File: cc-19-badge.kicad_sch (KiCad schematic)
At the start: 1 part

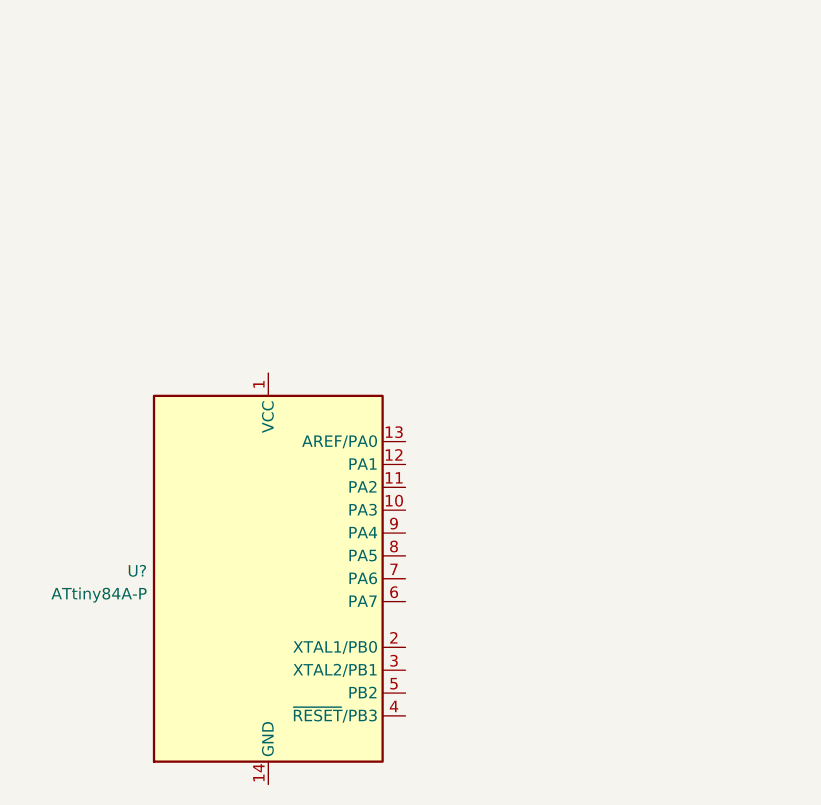
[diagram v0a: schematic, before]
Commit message: 9 make the pcb look like a beer can (#11)
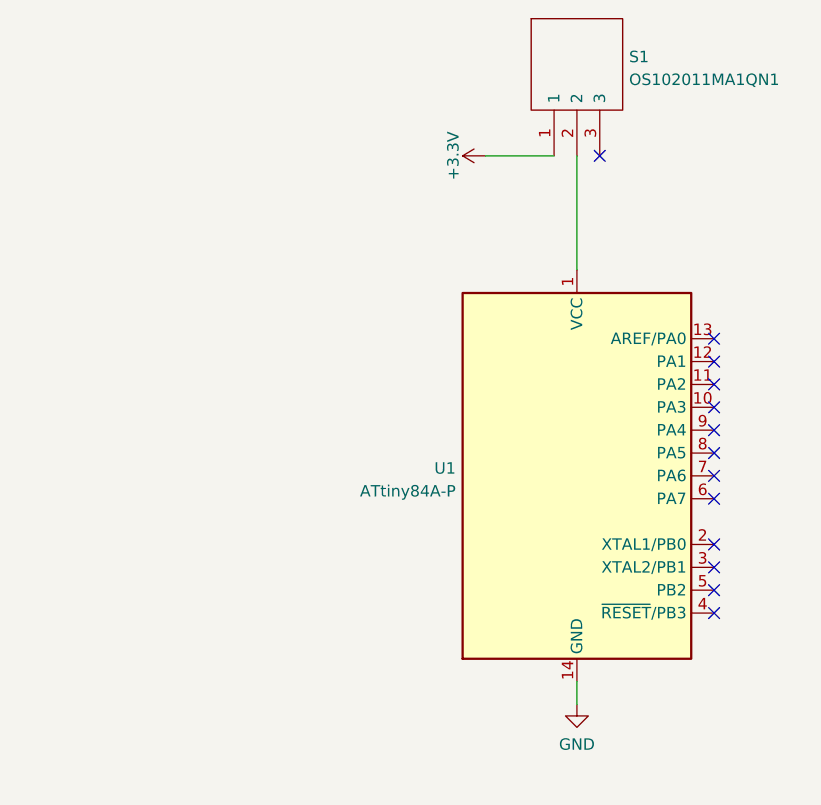
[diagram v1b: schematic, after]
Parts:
- removed U?: ATtiny84A-P, Package_DIP:DIP-14_W7.62mm, symbol MCU_Microchip_ATtiny:ATtiny84A-P
- added S1: OS102011MA1QN1, OS102011MA1QN1, symbol OS102011MA1QN1:OS102011MA1QN1
- added U1: ATtiny84A-P, Package_DIP:DIP-14_W7.62mm, symbol MCU_Microchip_ATtiny:ATtiny84A-P
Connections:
- new net: S1.2, U1.1 (VCC)
- new net +3.3V: S1.1
- new net GND: U1.14 (GND)
- no-connect marks 0 -> 13
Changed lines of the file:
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@@
 (kicad_sch (version 20211123) (generator eeschema)
   (paper "A4")
-  (symbol (lib_id "MCU_Microchip_ATtiny:ATtiny84A-P") (at 90.17 107.95 0) (unit 1)
+  (no_connect (at 139.7 96.52))
+  (no_connect (at 139.7 106.68))
+  (no_connect (at 139.7 81.28))
+  (no_connect (at 139.7 99.06))
+  (no_connect (at 139.7 109.22))
+  (no_connect (at 139.7 104.14))
+  (no_connect (at 139.7 91.44))
+  (no_connect (at 139.7 86.36))
+  (no_connect (at 139.7 93.98))
+  (no_connect (at 127 60.96))
+  (no_connect (at 139.7 88.9))
+  (no_connect (at 139.7 83.82))
+  (no_connect (at 139.7 111.76))
+  (wire (pts (xy 114.3 60.96) (xy 121.92 60.96))
+    (stroke (width 0) (type default) (color 0 0 0 0))
+  )
+  (wire (pts (xy 124.46 60.96) (xy 124.46 73.66))
+    (stroke (width 0) (type default) (color 0 0 0 0))
+  )
+  (wire (pts (xy 124.46 119.38) (xy 124.46 121.92))
+    (stroke (width 0) (type default) (color 0 0 0 0))
+  )
+  (symbol (lib_id "power:+3.3V") (at 114.3 60.96 90) (unit 1)
+    (in_bom yes) (on_board yes)
+    (property "Reference" "#PWR0102" (id 0) (at 118.11 60.96 0)
+      (effects (font (size 1.27 1.27)) hide)
+    )
+    (property "Value" "+3.3V" (id 1) (at 110.7242 60.96 0))
+    (property "Footprint" "" (id 2) (at 114.3 60.96 0)
+      (effects (font (size 1.27 1.27)) hide)
+    )
+    (property "Datasheet" "" (id 3) (at 114.3 60.96 0)
+      (effects (font (size 1.27 1.27)) hide)
+    )
+    (pin "1")
+  )
+  (symbol (lib_id "OS102011MA1QN1:OS102011MA1QN1") (at 121.92 60.96 0) (unit 1)
     (in_bom yes) (on_board yes) (fields_autoplaced)
-    (property "Reference" "U?" (id 0) (at 76.7081 107.1153 0)
+    (property "Reference" "S1" (id 0) (at 130.2512 49.9653 0)
+      (effects (font (size 1.27 1.27)) (justify left))
+    )
+    (property "Value" "OS102011MA1QN1" (id 1) (at 130.2512 52.5022 0)
+      (effects (font (size 1.27 1.27)) (justify left))
+    )
+    (property "Footprint" "OS102011MA1QN1" (id 2) (at 130.81 45.72 0)
+      (effects (font (size 1.27 1.27)) (justify left) hide)
+    )
+    (property "Datasheet" "http://www.ckswitches.com/media/1428/os.pdf" (id 3) (at 130.81 48.26 0)
+      (effects (font (size 1.27 1.27)) (justify left) hide)
+    )
+    (property "Description" "Switch Slide Right Angle SPDT 0.1A 12VDC Through Hole Slide Switch SPDT On-On 0.1 A@ 12 V dc Slide" (id 4) (at 130.81 50.8 0)
+      (effects (font (size 1.27 1.27)) (justify left) hide)
+    )
+    (property "Height" "" (id 5) (at 130.81 53.34 0)
+      (effects (font (size 1.27 1.27)) (justify left) hide)
+    )
+    (property "Mouser Part Number" "611-OS102011MA1QN1" (id 6) (at 130.81 55.88 0)
+      (effects (font (size 1.27 1.27)) (justify left) hide)
+    )
+    (property "Mouser Price/Stock" "https://www.mouser.co.uk/ProductDetail/CK/OS102011MA1QN1?qs=WtljUlYws5R6MUgHcLkz4w%3D%3D" (id 7) (at 130.81 58.42 0)
+      (effects (font (size 1.27 1.27)) (justify left) hide)
+    )
+    (property "Manufacturer_Name" "C & K COMPONENTS" (id 8) (at 130.81 60.96 0)
+      (effects (font (size 1.27 1.27)) (justify left) hide)
+    )
+    (property "Manufacturer_Part_Number" "OS102011MA1QN1" (id 9) (at 130.81 63.5 0)
+      (effects (font (size 1.27 1.27)) (justify left) hide)
+    )
+    (pin "1")
+    (pin "2")
+    (pin "3")
+  )
+  (symbol (lib_id "power:GND") (at 124.46 121.92 0) (unit 1)
+    (in_bom yes) (on_board yes) (fields_autoplaced)
+    (property "Reference" "#PWR0101" (id 0) (at 124.46 128.27 0)
+      (effects (font (size 1.27 1.27)) hide)
+    )
+    (property "Value" "GND" (id 1) (at 124.46 126.3634 0))
+    (property "Footprint" "" (id 2) (at 124.46 121.92 0)
+      (effects (font (size 1.27 1.27)) hide)
+    )
+    (property "Datasheet" "" (id 3) (at 124.46 121.92 0)
+      (effects (font (size 1.27 1.27)) hide)
+    )
+    (pin "1")
+  )
+  (symbol (lib_id "MCU_Microchip_ATtiny:ATtiny84A-P") (at 124.46 96.52 0) (unit 1)
+    (in_bom yes) (on_board yes) (fields_autoplaced)
+    (property "Reference" "U1" (id 0) (at 110.9981 95.6853 0)
       (effects (font (size 1.27 1.27)) (justify right))
     )
-    (property "Value" "ATtiny84A-P" (id 1) (at 76.7081 109.6522 0)
+    (property "Value" "ATtiny84A-P" (id 1) (at 110.9981 98.2222 0)
       (effects (font (size 1.27 1.27)) (justify right))
     )
-    (property "Footprint" "Package_DIP:DIP-14_W7.62mm" (id 2) (at 90.17 107.95 0)
+    (property "Footprint" "Package_DIP:DIP-14_W7.62mm" (id 2) (at 124.46 96.52 0)
       (effects (font (size 1.27 1.27) italic) hide)
     )
-    (property "Datasheet" "http://ww1.microchip.com/downloads/en/DeviceDoc/doc8183.pdf" (id 3) (at 90.17 107.95 0)
+    (property "Datasheet" "http://ww1.microchip.com/downloads/en/DeviceDoc/doc8183.pdf" (id 3) (at 124.46 96.52 0)
       (effects (font (size 1.27 1.27)) hide)
     )
@@
   )
   (symbol_instances
-    (path "/c53d2f4d-cfa3-4e34-aa9d-268fb6765344"
-      (reference "U?") (unit 1) (value "ATtiny84A-P") (footprint "Package_DIP:DIP-14_W7.62mm")
+    (path "/28701a8b-e9e9-4466-8fbd-2ff8d8c7af4f"
+      (reference "#PWR0101") (unit 1) (value "GND") (footprint "")
+    )
+    (path "/03b8bb26-888a-4324-a542-2f053d7430d1"
+      (reference "#PWR0102") (unit 1) (value "+3.3V") (footprint "")
+    )
+    (path "/040f8082-76ef-4eb1-ac5d-3018b40eb874"
+      (reference "S1") (unit 1) (value "OS102011MA1QN1") (footprint "OS102011MA1QN1")
+    )
+    (path "/b2e1ea54-795e-4622-b6af-e8674d527d3d"
+      (reference "U1") (unit 1) (value "ATtiny84A-P") (footprint "Package_DIP:DIP-14_W7.62mm")
     )
   )

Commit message: 20 update schematic (#22)
Co-authored-by: github-actions <github-actions@github.com>
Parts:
- added C1, C2: 100nF, third-party-schematics:K104K15X7RF5TH5, symbol K104K15X7RF5TH5:K104K15X7RF5TH5
- added C_RST1: 10uF, third-party-schematics:CAPPRD200W52D500H1250, symbol 860020372001:860020372001
- added IC1: ST25DV04KC-IE8S3, third-party-schematics:SOIC127P600X175-8N, symbol ST25DV04KC-IE8S3:ST25DV04KC-IE8S3
- added ISP1: Conn_02x03_Odd_Even, Connector_PinHeader_2.54mm:PinHeader_2x03_P2.54mm_Vertical, symbol Connector_Generic:Conn_02x03_Odd_Even
- added SCL_PULL1, SDA_PULL1: R_Small, symbol Device:R_Small
- S1: footprint OS102011MA1QN1 -> third-party-schematics:OS102011MA1QN1; Mouser Price/Stock https://www.mouser.co.uk/ProductDetail/CK/OS102011MA1QN1?qs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 -> https://www.mouser.com/ProductDetail/CK/OS102011MA1QN1?qs=W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
- U1: Mouser Part Number (none) -> 556-ATTINY84A-PU; Mouser Price/Stock (none) -> https://www.mouser.com/ProductDetail/Microchip-Technology-A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
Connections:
- net +3.3V: now also S1.2, U1.1 (VCC), C1.1, ISP1.2 (Pin_2); no longer S1.1
- net GND: now also C1.2, C2.2, C_RST1.2, IC1.4 (VSS), ISP1.6 (Pin_6)
- net at U1.11 (PA2): now also IC1.7 (GPO_(OPEN_DRAIN))
- net RST: now reaches U1.4 (~{RESET}/PB3)
- net RST: now also C_RST1.1, ISP1.5 (Pin_5)
- net MOSI: now reaches U1.7 (PA6)
- net MOSI: now also IC1.6 (SCL), ISP1.4 (Pin_4), SCL_PULL1.2
- net MISO: now reaches U1.8 (PA5)
- net MISO: now also ISP1.1 (Pin_1)
- net SCK: now reaches U1.9 (PA4)
- net SCK: now also IC1.5 (SDA), ISP1.3 (Pin_3), SDA_PULL1.2
- new net: C2.1, IC1.8 (VCC)
- new net +BATT: S1.1
- no-connect marks 13 -> 8
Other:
- moved on the sheet: S1, U1

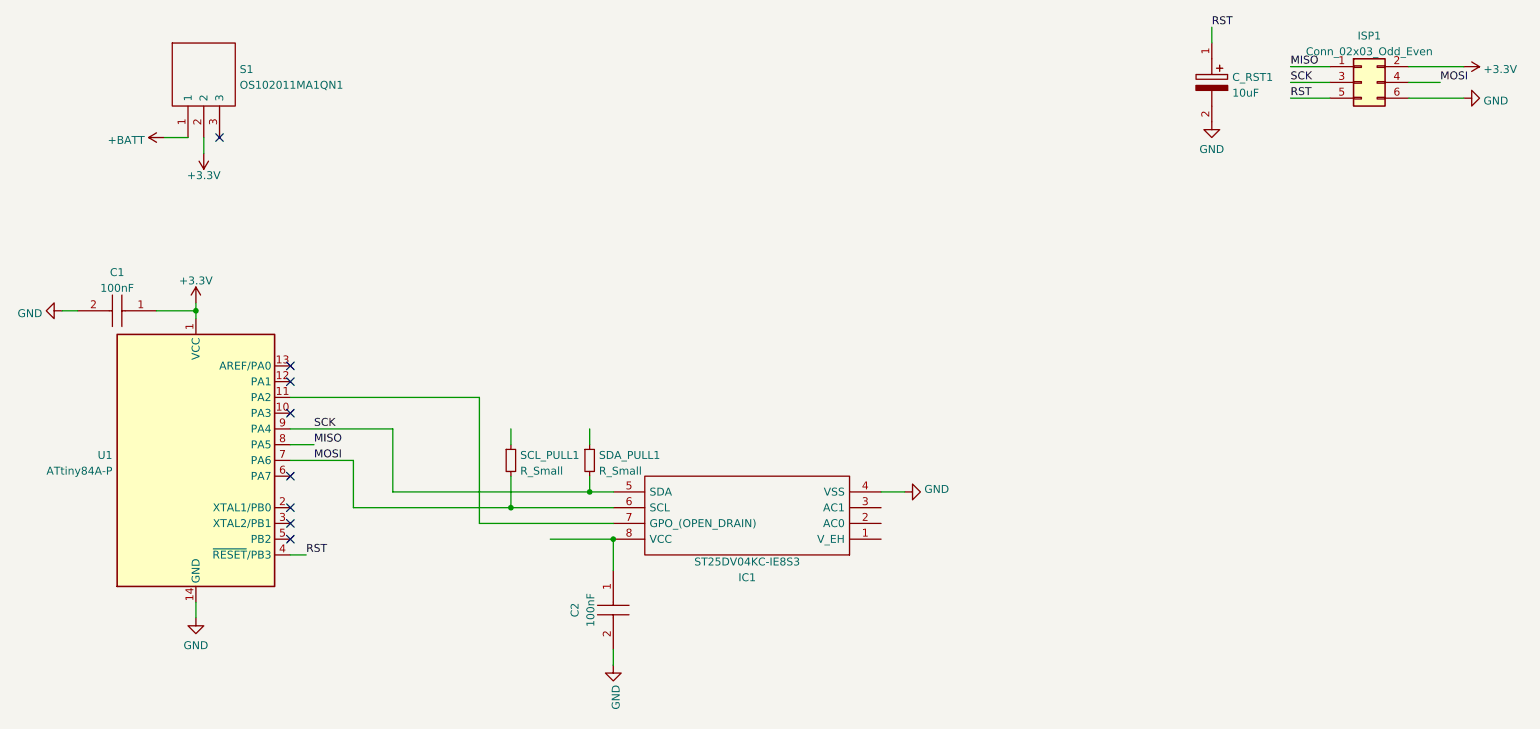
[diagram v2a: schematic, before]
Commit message: Add a 13.56 mhz antenna of questionable effectiveness  (#25)
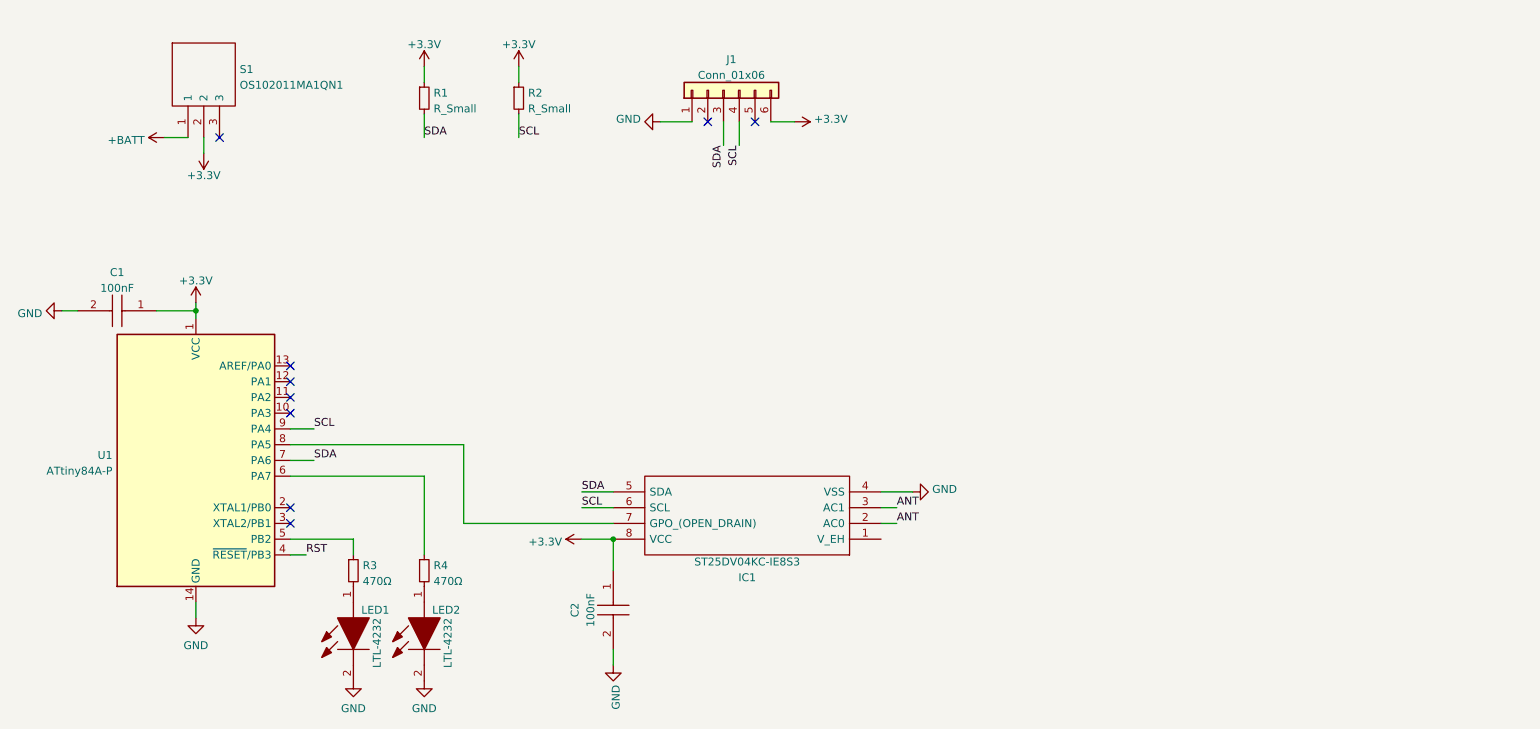
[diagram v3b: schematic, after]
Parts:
- removed C_RST1: 10uF, third-party-schematics:CAPPRD200W52D500H1250, symbol 860020372001:860020372001
- removed ISP1: Conn_02x03_Odd_Even, Connector_PinHeader_2.54mm:PinHeader_2x03_P2.54mm_Vertical, symbol Connector_Generic:Conn_02x03_Odd_Even
- removed SCL_PULL1, SDA_PULL1: R_Small, symbol Device:R_Small
- added J1: Conn_01x06, Connector_PinHeader_2.54mm:PinHeader_1x06_P2.54mm_Vertical, symbol Connector_Generic:Conn_01x06
- added LED1, LED2: LTL-4232, third-party-schematics:LTL4232, symbol LTL-4232:LTL-4232
- added R1, R2: R_Small, third-party-schematics:CFR-Resistor, symbol Device:R_Small
- added R3, R4: 470Ω, third-party-schematics:CFR-Resistor, symbol Device:R_Small
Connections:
- net +3.3V: now also C2.1, IC1.8 (VCC), J1.6 (Pin_6), R1.1, R2.1
- net GND: now also J1.1 (Pin_1), LED1.2, LED2.2
- net at U1.11 (PA2): no longer IC1.7 (GPO_(OPEN_DRAIN))
- net at U1.5 (PB2): now also R3.1
- net at U1.6 (PA7): now also R4.1
- net ANT: now reaches IC1.2 (AC0)
- net ANT: now also IC1.3 (AC1)
- net MISO: no longer names the net of U1.8 (PA5)
- net MISO: now also IC1.7 (GPO_(OPEN_DRAIN))
- net MOSI renamed SCL
- net SCL: now also U1.9 (PA4), J1.4 (Pin_4), R2.2; no longer U1.7 (PA6)
- net SCK renamed SDA
- net SDA: now also U1.7 (PA6), J1.3 (Pin_3), R1.2; no longer U1.9 (PA4)
- new net: LED2.1, R4.2
- new net: LED1.1, R3.2
- no-connect marks 8 -> 9

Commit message: 31 use attiny85 20pu (#33)
Co-authored-by: github-actions <github-actions@github.com>
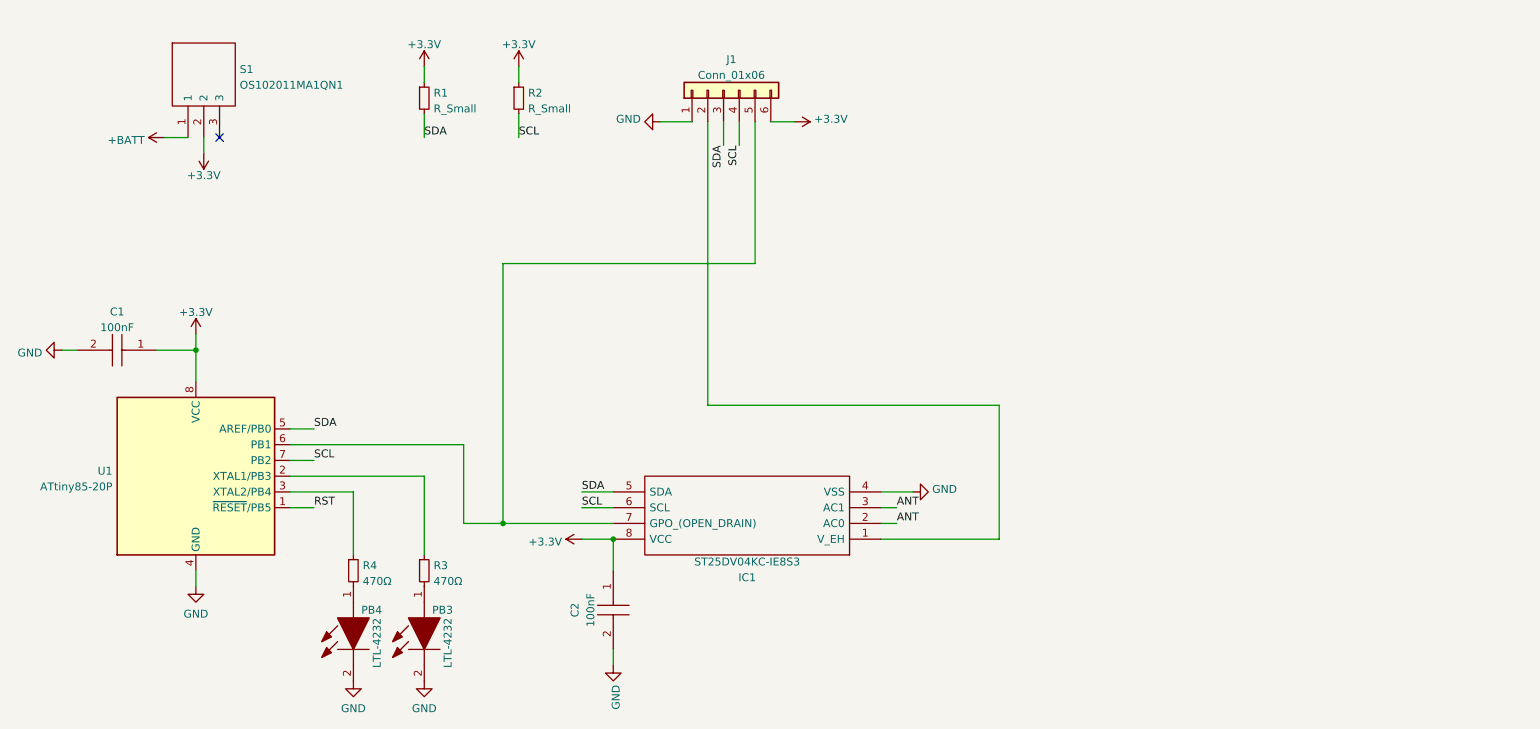
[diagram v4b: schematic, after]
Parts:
- removed U1: ATtiny84A-P, Package_DIP:DIP-14_W7.62mm, symbol MCU_Microchip_ATtiny:ATtiny84A-P
- added U1: ATtiny85-20P, Package_DIP:DIP-8_W7.62mm, symbol MCU_Microchip_ATtiny:ATtiny85-20P
- renumbered LED2 to PB3, LED1 to PB4, R4 to R3, R3 to R4
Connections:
- net +3.3V: now also U1.8 (VCC)
- net GND: now also U1.4 (GND)
- net RST: now also U1.1 (~{RESET}/PB5)
- net SCL: now also U1.7 (PB2)
- net SDA: now also U1.5 (AREF/PB0)
- net at R3.1: now also U1.2 (XTAL1/PB3)
- net at J1.2 (Pin_2): now also IC1.1 (V_EH)
- net at J1.5 (Pin_5): now also IC1.7 (GPO_(OPEN_DRAIN)), U1.6 (PB1)
- net at R4.1: now also U1.3 (XTAL2/PB4)
- no-connect marks 9 -> 1
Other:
- moved on the sheet: C1

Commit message: hello
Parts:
- removed C1: 100nF, third-party-schematics:K104K15X7RF5TH5, symbol K104K15X7RF5TH5:K104K15X7RF5TH5
- removed PB3, PB4: LTL-4232, third-party-schematics:LTL4232, symbol LTL-4232:LTL-4232
- removed R3, R4: 470Ω, third-party-schematics:CFR-Resistor, symbol Device:R_Small
- removed U1: ATtiny85-20P, Package_DIP:DIP-8_W7.62mm, symbol MCU_Microchip_ATtiny:ATtiny85-20P
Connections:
- net SCL: now also J1.3 (Pin_3); no longer J1.4 (Pin_4)
- net SDA: now also J1.2 (Pin_2); no longer J1.3 (Pin_3)
- net at IC1.1 (V_EH): now also J1.5 (Pin_5); no longer J1.2 (Pin_2)
- net at IC1.7 (GPO_(OPEN_DRAIN)): now also J1.4 (Pin_4); no longer J1.5 (Pin_5)

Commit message: new NFC IC
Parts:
- removed IC1: ST25DV04KC-IE8S3, third-party-schematics:SOIC127P600X175-8N, symbol ST25DV04KC-IE8S3:ST25DV04KC-IE8S3
- removed R1, R2: R_Small, third-party-schematics:CFR-Resistor, symbol Device:R_Small
- added IC1: M24SR16-YDW6T_2, SOP65P640X120-8N, symbol M24SR16-YDW6T_2:M24SR16-YDW6T_2
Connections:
- net +3.3V: now also IC1.8 (VCC)
- net ANT: now also IC1.2 (AC0), IC1.3 (AC1)
- net GND: now also IC1.4 (VSS)
- net SCL: now also IC1.6 (SCL)
- net SDA: now also IC1.5 (SDA)
- net at J1.4 (Pin_4): now also IC1.7 (GPO)
- net at J1.5 (Pin_5): now also IC1.1 (RF_DISABLE)
